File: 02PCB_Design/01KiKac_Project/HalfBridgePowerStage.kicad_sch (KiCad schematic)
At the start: 24 parts, among them U5 LMG2100R044RARR, U6 INA240A1PW

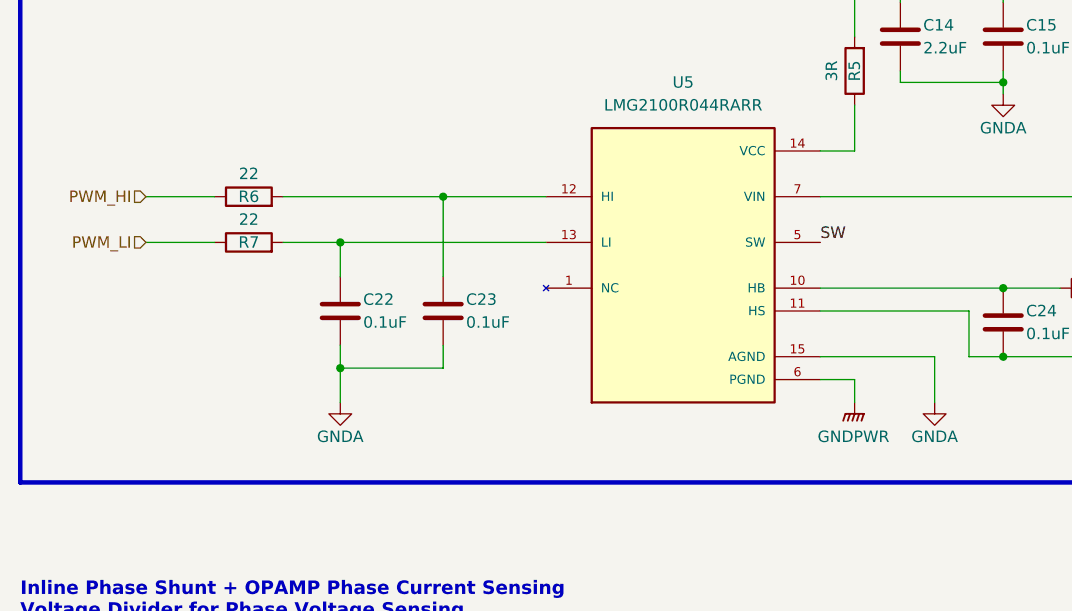
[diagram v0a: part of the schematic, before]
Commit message: added CAN + minor changes
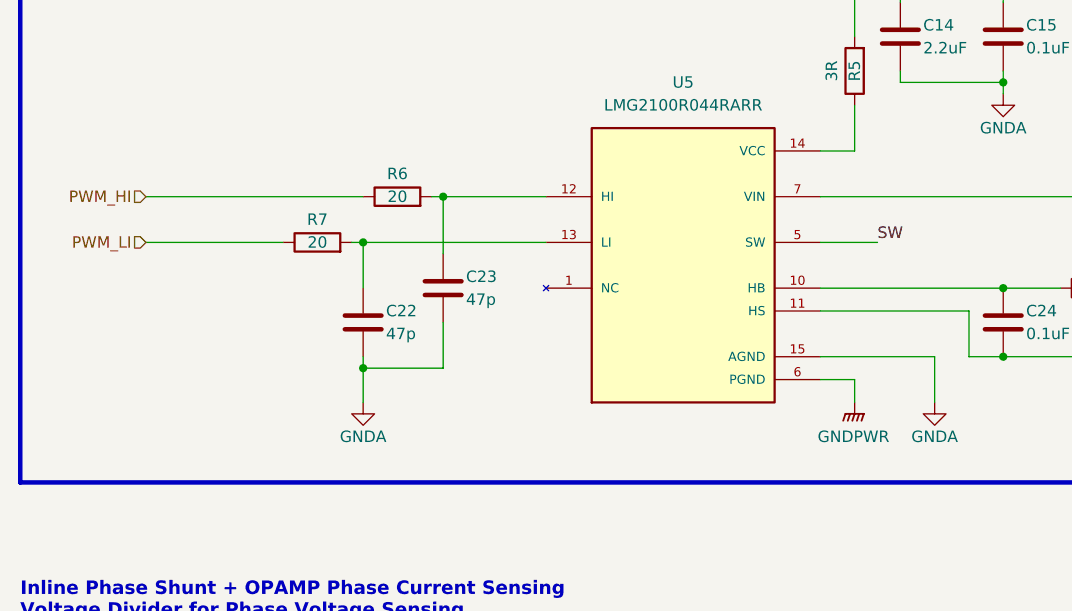
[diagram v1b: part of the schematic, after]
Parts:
- C22, C23: value 0.1uF -> 47p
- R6, R7: value 22 -> 20
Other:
- moved on the sheet: C22, C23, R6, R7

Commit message: cleanup
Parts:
- renumbered C14 to C17, C15 to C18, C16 to C19, C17 to C20, C18 to C21, C19 to C22, C20 to C23, C21 to C24, C23 to C25, C22 to C26, C24 to C27, C25 to C28, C26 to C29, C27 to C30, C28 to C31, R5 to R10, R6 to R11, R7 to R12, R8 to R13, R9 to R14, R10 to R15, R11 to R16
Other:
- moved on the sheet: C17, C18, C19, C20, C21, C22, C23, C24, C25, C26, C27, C28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
